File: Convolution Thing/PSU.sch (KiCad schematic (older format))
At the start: 8 parts

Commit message: Just EE things
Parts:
- added C? (x2): 100nF, symbol Device:C
- added C?: 10uF, symbol Device:C
- added C?: 10nF, symbol Device:C
- added D? (x2): Schottky, symbol Device:D_Schottky
- added TP?: +12V TP, symbol Connector:TestPoint
- added TP?: -12V TP, symbol Connector:TestPoint
- added TP?: +3.3V TP, symbol Connector:TestPoint
- added TP?: +3.3VA TP, symbol Connector:TestPoint
- added TP?: +5V TP, symbol Connector:TestPoint
- added TP?: PowerGood TP, symbol Connector:TestPoint
- added U?: Compute_Module_4_Functional, symbol CM4:Compute_Module_4_Functional
- added U?: TLV1117-33, symbol Regulator_Linear:TLV1117-33
- C?: value 10u -> 10uF
- D?: value Schottky -> SSA33L
- L?: value 10U -> 10uH
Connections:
- net labels added: +3.3V, +3.3VA, PowerGood
- wire segments 26 -> 64
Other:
- moved on the sheet: C?, D?, J?, U?

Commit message: Convolution Thing PCB design continues
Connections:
- no-connect marks 0 -> 2
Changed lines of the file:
@@
 $Descr A4 11693 8268
 encoding utf-8
-Sheet 3 4
+Sheet 3 7
 Title ""
 Date ""
@@
 Wire Wire Line
 	5700 2550 5950 2550
+NoConn ~ 2550 3000
+NoConn ~ 2550 3100
 $EndSCHEMATC

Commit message: Work on CODEC and In/Out stages
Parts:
- removed C?: 10nF, symbol Device:C
- added C?: 10uf, symbol Device:CP1
- added C?: 100uf, symbol Device:CP1
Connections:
- wire segments 64 -> 65
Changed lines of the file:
@@
 L power:+5V #PWR?
 U 1 1 61083815
-P 1250 4050
-F 0 "#PWR?" H 1250 3900 50  0001 C CNN
-F 1 "+5V" H 1100 4150 50  0000 C CNN
-F 2 "" H 1250 4050 50  0001 C CNN
-F 3 "" H 1250 4050 50  0001 C CNN
-	1    1250 4050
-	1    0    0    -1
-$EndComp
-Wire Wire Line
-	1250 4050 1350 4050
+P 1000 4050
+F 0 "#PWR?" H 1000 3900 50  0001 C CNN
+F 1 "+5V" H 850 4150 50  0000 C CNN
+F 2 "" H 1000 4050 50  0001 C CNN
+F 3 "" H 1000 4050 50  0001 C CNN
+	1    1000 4050
+	1    0    0    -1
+$EndComp
 Wire Wire Line
 	1350 1550 2050 1550
@@
 	1    0    0    -1
 $EndComp
-$Comp
-L Device:C C?
-U 1 1 610B3F67
-P 2200 4200
-F 0 "C?" H 2315 4246 50  0000 L CNN
-F 1 "10nF" H 2315 4155 50  0000 L CNN
-F 2 "" H 2238 4050 50  0001 C CNN
-F 3 "~" H 2200 4200 50  0001 C CNN
-	1    2200 4200
-	1    0    0    -1
-$EndComp
 Connection ~ 2200 4050
 $Comp
@@
 NoConn ~ 2550 3000
 NoConn ~ 2550 3100
+$Comp
+L power:GND #PWR?
+U 1 1 61070140
+P 1150 4350
+F 0 "#PWR?" H 1150 4100 50  0001 C CNN
+F 1 "GND" H 1155 4177 50  0000 C CNN
+F 2 "" H 1150 4350 50  0001 C CNN
+F 3 "" H 1150 4350 50  0001 C CNN
+	1    1150 4350
+	1    0    0    -1
+$EndComp
+Wire Wire Line
+	1000 4050 1150 4050
+$Comp
+L Device:CP1 C?
+U 1 1 6107C671
+P 1150 4200
+F 0 "C?" H 900 4250 50  0000 L CNN
+F 1 "10uf" H 850 4150 50  0000 L CNN
+F 2 "" H 1150 4200 50  0001 C CNN
+F 3 "~" H 1150 4200 50  0001 C CNN
+	1    1150 4200
+	1    0    0    -1
+$EndComp
+Connection ~ 1150 4050
+Wire Wire Line
+	1150 4050 1350 4050
+$Comp
+L Device:CP1 C?
+U 1 1 6107E7C5
+P 2200 4200
+F 0 "C?" H 2350 4250 50  0000 L CNN
+F 1 "100uf" H 2350 4150 50  0000 L CNN
+F 2 "" H 2200 4200 50  0001 C CNN
+F 3 "~" H 2200 4200 50  0001 C CNN
+	1    2200 4200
+	1    0    0    -1
+$EndComp
 $EndSCHEMATC

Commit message: New stereo codec and related changes. RIP multi-channel audio.
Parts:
- removed C?: 100nF, symbol Device:C_Small
- removed C? (x2): 22uF, symbol Device:C
- removed C? (x2): 10uF, symbol Device:C
- removed C? (x2): 100nF, symbol Device:C
- removed D?: SSA33L, symbol Device:D_Schottky
- removed L?: 10uH, symbol Device:L
- removed TP?: +5V TP, symbol Connector:TestPoint
- removed TP?: PowerGood TP, symbol Connector:TestPoint
- removed U?: ADP2302ARDZ-5.0, Package_SO:SOIC-8-1EP_3.9x4.9mm_P1.27mm_EP2.29x3mm, symbol Regulator_Switching:ADP2302ARDZ-5.0
- removed U?: TLV1117-33, symbol Regulator_Linear:TLV1117-33
- added C? (x3): 10uF, symbol Device:CP1
- added C?: 10uf, symbol Device:CP1
- added C?: 100uf, symbol Device:CP1
- added D? (x2): D, symbol Device:D
- added TP?: GND TP, symbol Connector:TestPoint
- added TP?: +5VA TP, symbol Connector:TestPoint
- added U? (x2): TLV1117-50, symbol Regulator_Linear:TLV1117-50
- TP?: value +3.3VA TP -> +5V TP
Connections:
- net labels added: +5VA
- net labels removed: +3.3VA, PowerGood
- wire segments 65 -> 53
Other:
- moved on the sheet: C?, D?, TP?

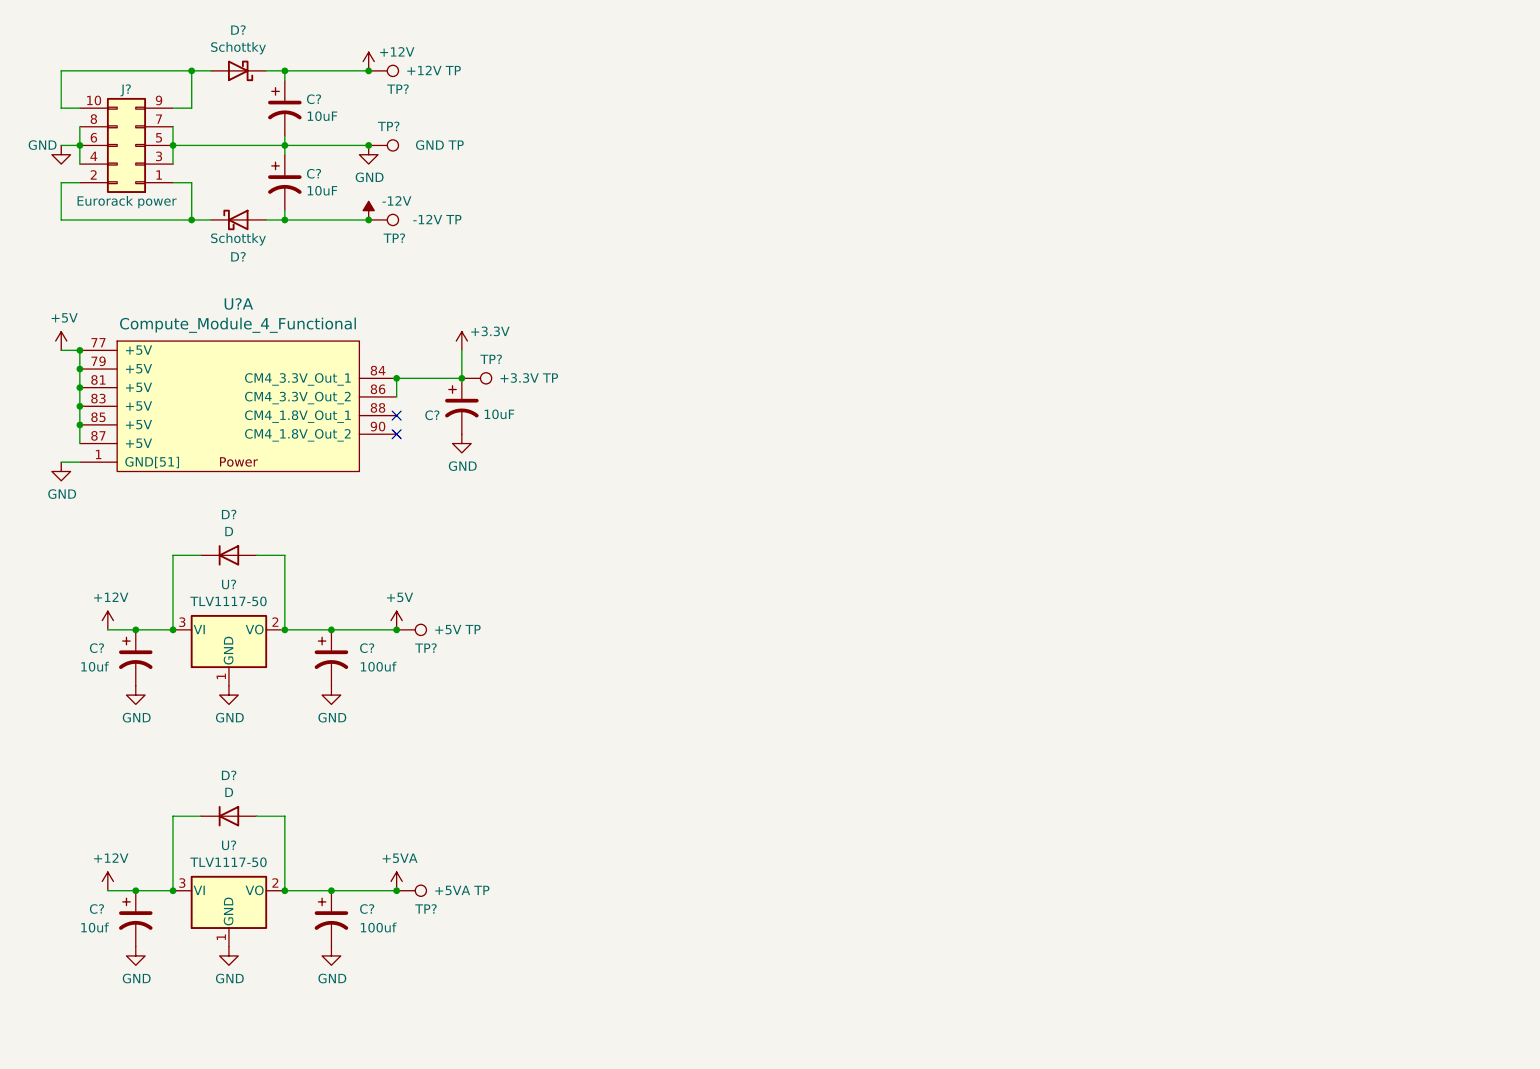
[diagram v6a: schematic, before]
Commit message: Added gate inputs and CM4 / display sockets, made CV inputs 100k, lots of smaller changes. First iteration of schematic now done.
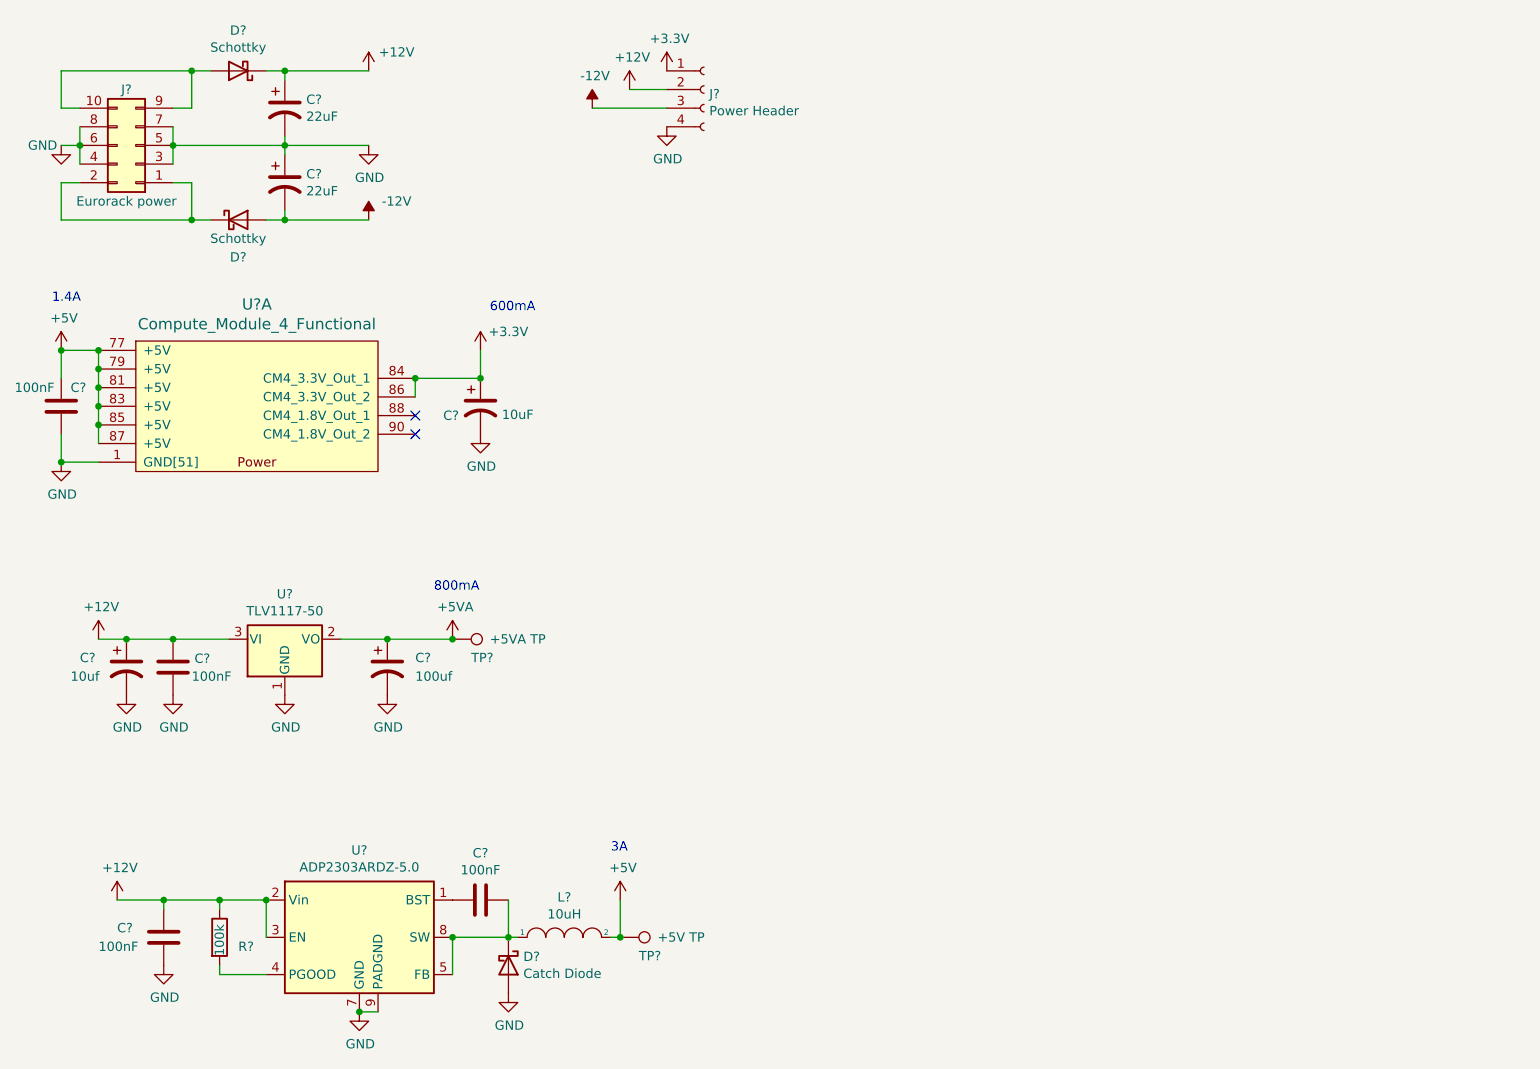
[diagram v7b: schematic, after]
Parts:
- removed C?: 10uf, symbol Device:CP1
- removed C?: 100uf, symbol Device:CP1
- removed D? (x2): D, symbol Device:D
- removed TP?: GND TP, symbol Connector:TestPoint
- removed TP?: +12V TP, symbol Connector:TestPoint
- removed TP?: -12V TP, symbol Connector:TestPoint
- removed TP?: +3.3V TP, symbol Connector:TestPoint
- removed TP?: +5V TP, symbol Connector:TestPoint
- removed U?: TLV1117-50, symbol Regulator_Linear:TLV1117-50
- added C? (x4): 100nF, symbol Device:C
- added D?: Catch Diode, symbol Device:D_Schottky
- added J?: Power Header, symbol Connector:Conn_01x04_Female
- added L?: 10uH, symbol pspice:INDUCTOR
- added R?: 100k, symbol Device:R
- added TP?: +5V TP, symbol Connector:TestPoint
- added U?: ADP2303ARDZ-5.0, Package_SO:SOIC-8-1EP_3.9x4.9mm_P1.27mm_EP2.29x3mm, symbol Regulator_Switching:ADP2303ARDZ-5.0
- C? (x2): value 10uF -> 22uF
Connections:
- net +12V: now also C?.1, C?.1, J?.2 (Pin_2), R?.1, U?.2 (Vin), U?.3 (EN)
- net +3V3: now also J?.1 (Pin_1)
- net +5V: now also C?.1, L?.2, TP?.1
- net -12V: now also J?.3 (Pin_3)
- net GND: now also C?.2, C?.2, C?.2, D?.2 (A), J?.4 (Pin_4), U?.7 (GND), U?.9 (PADGND)
- new net: R?.2, U?.4 (PGOOD)
- new net: C?.1, D?.1 (K), L?.1, U?.5 (FB), U?.8 (SW)
- new net: C?.2, U?.1 (BST)
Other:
- note added: "1.4A"
- note added: "3A"
- note added: "600mA"
- note added: "800mA"
- moved on the sheet: C?, TP?, U?, U?A

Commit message: Fix some issues, add component references
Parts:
- gave numbers to parts that had none: 21
